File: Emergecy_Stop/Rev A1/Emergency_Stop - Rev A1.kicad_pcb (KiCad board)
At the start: 2 copper layers, 55 x 25 mm, 13 parts, among them J1 XLR3, J2 XLR3, J3 CONN_01X02_FEMALE

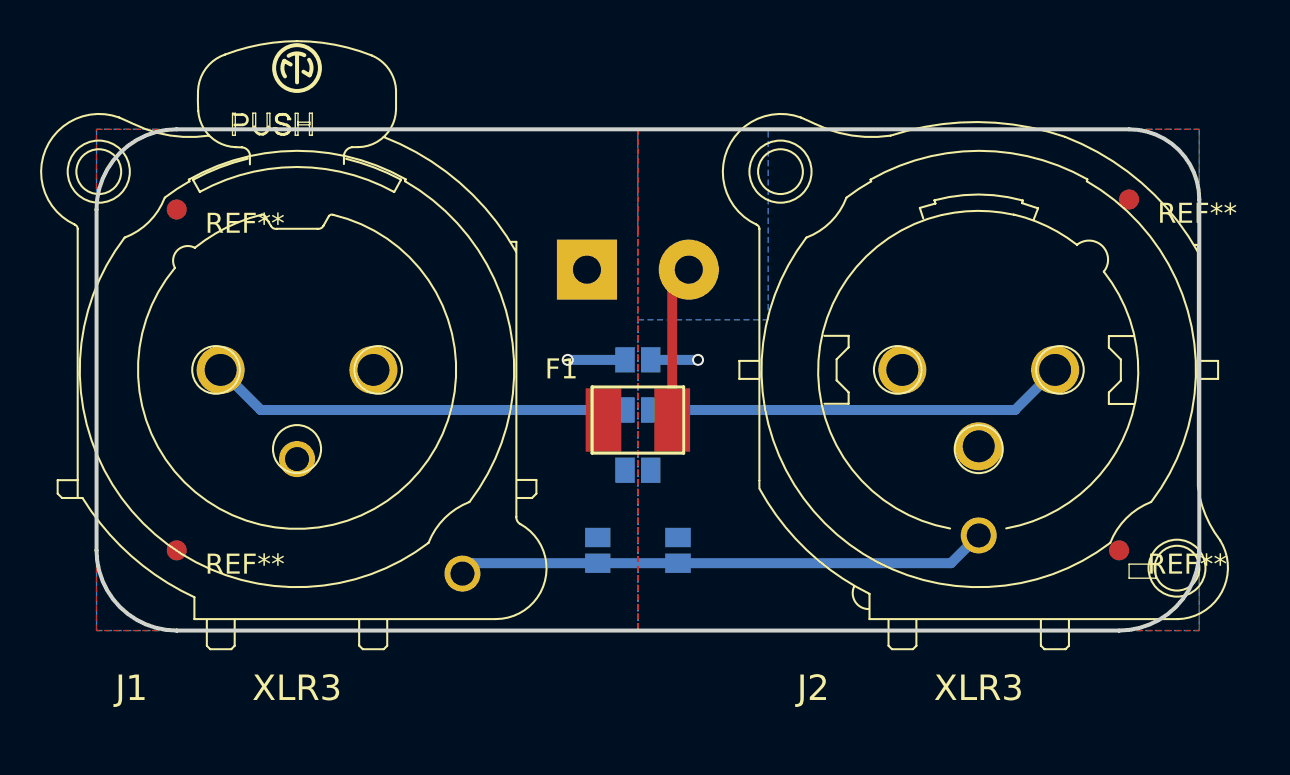
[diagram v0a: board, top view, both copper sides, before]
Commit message: Modify power connector
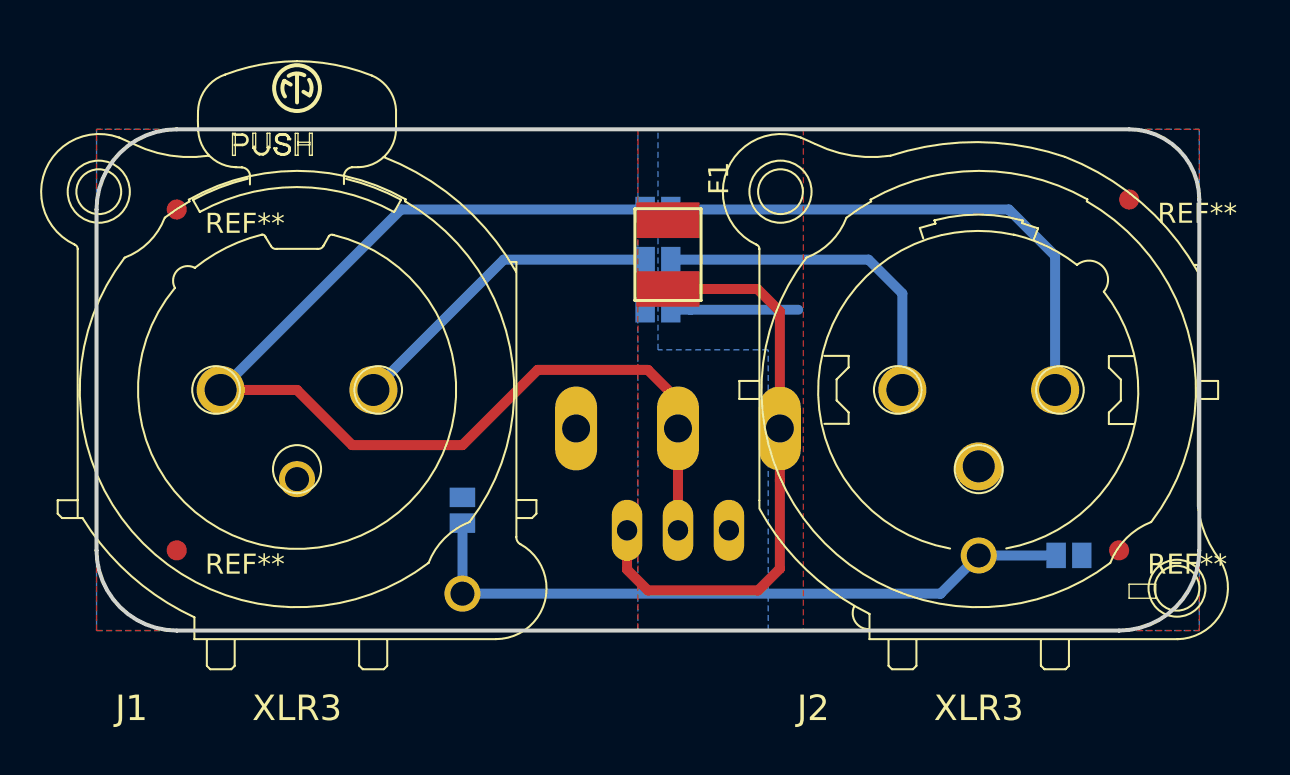
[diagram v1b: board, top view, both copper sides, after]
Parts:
- added J4: CONN_01X03_FEMALE, conn_Molex:7395-03, B.Cu at (119.0, 108.0)
- J3: value CONN_01X02_FEMALE -> CONN_01X03_FEMALE; footprint test:MSTBA2.5 -> conn_Phoenix:MSTBA3
- moved JP5 19.5 mm to (138.5, 109.2), turned to 270 degrees
- moved J3 17.1 mm to (119.0, 108.0), turned to 180 degrees
- moved JP2 10.0 mm to (118.0, 92.0)
- moved F1 8.39 mm to (118.5, 94.2), turned to 270 degrees
- moved JP3 8.06 mm to (118.0, 97.0)
- moved JP4 7.04 mm to (108.2, 107.0)
- moved JP1 5.10 mm to (118.0, 94.5)
- moved J1 1.00 mm to (100.0, 101.0)
- moved J2 1.00 mm to (134.0, 101.0)
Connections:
- F1 pad 2: /GND_IN -> /+24V
- J3 pad 1: /24V_IN -> /+24V
- J3 pad 2: /GND_IN -> /SIG_IN
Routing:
- net /SIG_IN: track 21.0 -> 57.5 mm
- net /+24V: track 0.00 -> 29.3 mm
- net /24V_OUT: track 2.36 -> 17.1 mm, vias 1 -> 0
- net /24V_IN: track 2.86 -> 16.2 mm, vias 1 -> 0
- net /GND_IN: track 7.84 -> 0.00 mm
- net /GND_MECA: track 26.5 -> 33.9 mm
- net /GND_OUT: track 0.00 -> 6.36 mm
- net /SIG_OUT: track 21.0 -> 26.8 mm

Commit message: Finishing emergency stop board and generate MDP folder
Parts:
- added S?: CC-BY-NC-SA, CC-BY-NC-SA, B.Cu at (102.5, 95.0)
- added T3: EXMACHINA-LOGO-NAME, EXM-LOGO-BASELINE, B.Cu at (138.0, 95.0)
- F1: value Fuse -> 1812L110/24DR
- J1: footprint Neutrix:NC3FAV2 -> NC3FAV2
- J2: footprint Neutrix:NC3MAV -> NC3MAV
- J3: value CONN_01X03_FEMALE -> MSTBA2.5/3; footprint conn_Phoenix:MSTBA3 -> MSTBA3
- J4: value CONN_01X03_FEMALE -> 22-05-7038; footprint conn_Molex:7395-03 -> 22-05-7038
- REF** (x4): value Fiducial_1mm_Dia_2.54mm_Outer_CopperTop -> Fiducial
- moved F1 1.52 mm to (117.0, 94.0), turned to 0 degrees
- turned JP4 to 90 degrees
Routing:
- net /24V_IN: track 16.2 -> 19.1 mm
- net /SIG_IN: track 57.5 -> 59.7 mm
- net /+24V: track 29.3 -> 30.8 mm
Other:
- board text added: "Emergency Stop Rev A1"

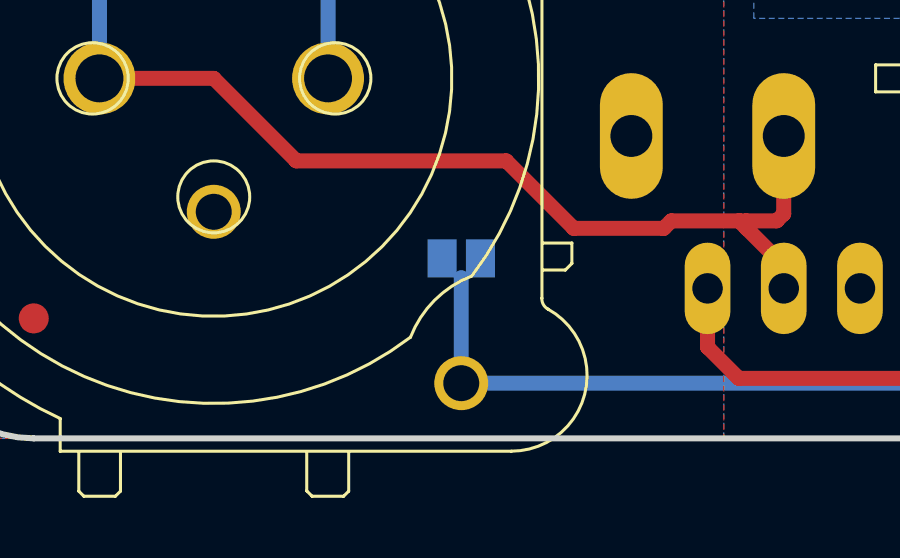
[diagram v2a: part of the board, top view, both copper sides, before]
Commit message: Move JP4 and route the GND_MECA
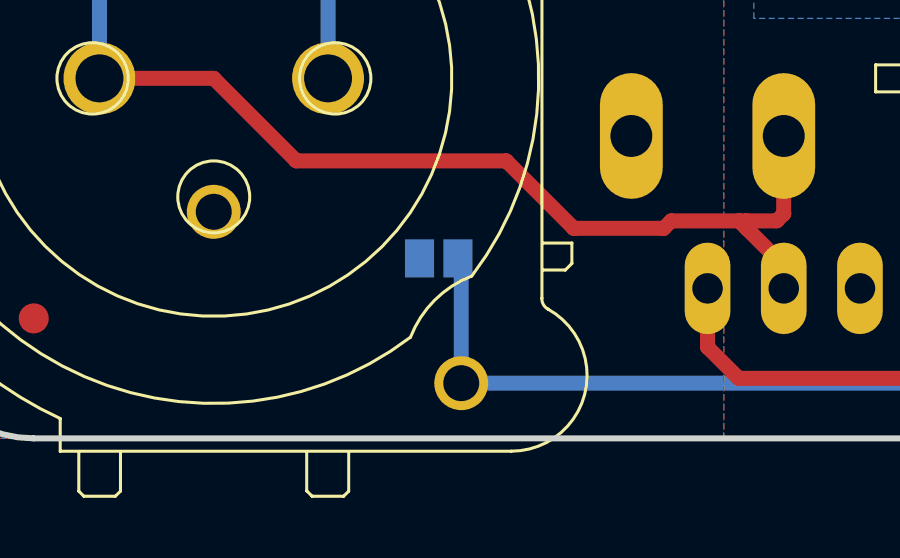
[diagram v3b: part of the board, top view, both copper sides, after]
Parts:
- moved JP4 0.75 mm to (107.5, 107.0)
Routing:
- net /GND_MECA: track 33.9 -> 34.6 mm
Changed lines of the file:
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@@
   (general
     (links 18)
-    (no_connects 0)
+    (no_connects 2)
     (area 89.899999 87.899999 145.100001 113.100001)
     (thickness 1.6)
     (drawings 11)
-    (tracks 45)
+    (tracks 46)
     (zones 0)
     (modules 16)
@@
   (page A4)
   (layers
-    (0 F.Cu signal hide)
-    (31 B.Cu signal hide)
+    (0 F.Cu signal)
+    (31 B.Cu signal)
     (32 B.Adhes user)
     (33 F.Adhes user)
@@
   )
   (module Connect:GS2 (layer B.Cu)
-    (at 108.25 107 90)
+    (at 107.5 107 90)
     (descr "2-pin solder bridge")
     (tags "solder bridge")
@@
   (segment (start 119.625 97) (end 125 97) (width 0.5) (layer B.Cu) (net 6))
   (segment (start 118.64 97) (end 119.625 97) (width 0.5) (layer B.Cu) (net 6))
+  (segment (start 108.24992 111.16) (end 108.24992 107.10992) (width 0.5) (layer B.Cu) (net 7))
+  (segment (start 108.24992 107.10992) (end 108.14 107) (width 0.5) (layer B.Cu) (net 7))
   (segment (start 108.24992 111.16) (end 132.095 111.16) (width 0.5) (layer B.Cu) (net 7))
   (segment (start 132.095 111.16) (end 134 109.255) (width 0.5) (layer B.Cu) (net 7))
   (segment (start 134 109.255) (end 137.855 109.255) (width 0.5) (layer B.Cu) (net 7))
   (segment (start 137.855 109.255) (end 137.86 109.25) (width 0.5) (layer B.Cu) (net 7))
-  (segment (start 108.25 107.64) (end 108.25 111.15992) (width 0.5) (layer B.Cu) (net 7))
   (segment (start 108.25 111.15992) (end 108.24992 111.16) (width 0.5) (layer B.Cu) (net 7))
   (segment (start 118.7145 94) (end 122.5 94) (width 0.5) (layer F.Cu) (net 8))
